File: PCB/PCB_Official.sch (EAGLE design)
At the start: 66 parts, among them IC1 MCP73871, U1 TPS63070, U2 STM32F767ZIT6, U3 STM32L053C8T6, U4 TPS63070, U5 BATTERY-MANAGEMENT-TEMP_BQ274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

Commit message: Schematic almost finalized
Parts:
- added C23, C24: 2.2uF, rcl:C-USC0805
- added C25: 10nF, rcl:C-USC0805
- added C26, C27, C28, C29, C30, C31, C32, C33, C34, C35, C36, C37, C43, C44, C45, C46, C47: 100nF, rcl:C-USC0805
- added C38: 4.7uF, rcl:C-USC0805
- added C39, C40, C41, C42: 4.3pF, rcl:C-USC0805
- added C48: 1uF, rcl:C-USC0805
- added J3: 455-1750-1-ND, SparkFun-Connectors:CONN_03
- added Q1: 220mA/50V/3.5Ω, SparkFun-DiscreteSemi:MOSFET-NCH-BSS138
- added R21, R22, R23, R24: 10k, rcl:R-US_R0805
- added SOLAR: (no value), adafruit:JST_2PIN-SMT-RA
- J1: device SparkFun-Connectors:CONN_11 -> SparkFun-Connectors:CONN_13
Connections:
- removed net N$32: J1.4
- new net DCMI_D2: J1.5, U2PC.PC8(TRACED1,TIM3_CH3,TIM8_CH3,UART5_RTS,USART6_CK,FMC_NE2/FMC_NCE,SDMMC1_D0,DCMI_D2)
- new net DCMI_D3: J1.6, U2PC.PC9(MCO2,TIM3_CH4,TIM8_CH4,I2S3_SDA,I2S_CKIN,UART5_CTS,QUADSPI_BK1_IO0,LCD_G3,SDMMC12_D1,DCMI_D3,LCD_B2)
- new net DCMI_D4: J1.7, U2PC.PC11(DFSDM1_DATIN5,SPI3_MISO,USART3_RX,UART4_RX,QUADSPI_BK2_NCS,SDMMC1_D3,DCMI_D4)
- new net DCMI_D5: J1.8, U2PD.PD3(DFSDM1_CKOUT,SPI2_SCK/I2S2_CK,DFSDM1_DATIN0,USART2_CTS,FMC_CLK,DCMI_D5,LCD_G7)
- new net DCMI_D6: J1.9, U2PB.PB8(I2C4_SCL,TIM4_CH3,TIM10_CH1,I2C1_SCL,DFSDM1_CKIN7,UART5_RX,CAN1_RX,SDMMC2_D4,ETH_MII_TXD3,SDMMC1_D4,DCMI_D6,LCD_B6)
- new net DCMI_D7: J1.10, U2PB.PB9(I2C4_SDA,TIM4_CH4,TIM11_CH1,I2C1_SDA,SPI2_NSS/I2S2_WS,DFSDM1_DATIN7,UART5_TX,CAN1_TX,SDMMC2_D5,I2C4_SMBA,SDMMC1_D5,DCMI_D7,LCD_B7)
- new net DCMI_VSYNC: J1.11, U2PG.PG9(SPI1_MISO,SPDIF_RX3,USART6_RX,QUADSPI_BK2_IO2,SAI2_FS_B,SDMMC2_D0,FMC_NE2/FMC_NCE,DCMI_VSYNC)
- new net F7_RX: MCU_UART.4, U2PA.PA1(TIM2_CH2,TIM5_CH2,USART2_RTS,UART4_RX,QUADSPI_BK1_IO3,SAI2_MCLK_B,ETH_MII_RX_CLK/ETH_RMII_REF_CLK,LCD_R2)
- new net F7_TX: MCU_UART.2, U2PA.PA0-WKUP(TIM2_CH1/TIM2_ETR,TIM5_CH1,TIM8_ETR,USART2_CTS,UART4_TX,SAI2_SD_B,ETH_MII_CRS,ADC1_IN0,ADC2_IN0,ADC3_IN0,WKUP1)
- new net GSM_RST: U$1.RST, U3.PB5
- new net I2C_SCL: J1.13, U2PB.PB6(UART5_TX,TIM4_CH1,HDMI_CEC,I2C1_SCL,DFSDM1_DATIN5,USART1_TX,CAN2_TX,QUADSPI_BK1_NCS,I2C4_SCL,FMC_SDNE1,DCMI_D5)
- new net I2C_SDA: J1.12, U2PB.PB7(TIM4_CH2,I2C1_SDA,DFSDM1_CKIN5,USART1_RX,I2C4_SDA,FMC_NL,DCMI_VSYNC)
- new net L0_RX: MCU_UART.1, U3.PB11
- new net L0_SWCLK: L0_PROGRAM.3, U3.PA14
- new net L0_SWDIO: L0_PROGRAM.2, U3.PA13
- new net L0_TX: MCU_UART.3, U3.PB10
- new net LORA_INT: U$9.G0, U3.PB6
- new net LORA_RST: U$9.RST, U3.PB7
- new net MCU_RST: J2.4, L0_PROGRAM.4, U2PWR_CONTR.NRST, U3.NRST
- new net SYS_JTCK_SWCLK: J2.3, U2PA.PA14(JTCK-SWCLK)
- new net SYS_JTMS_SWDIO: J2.2, U2PA.PA13(JTMS-SWDIO)
- new net TIM3_CH2: Q1.S, R22.1
- new net VCAP1: C23.1, U2PWR_CONTR.VCAP_1
- new net VCAP2: C24.1, U2PWR_CONTR.VCAP_2
- net +3V3: now also C25.1, C26.1, C27.1, C28.1, C29.1, C30.1, C31.1, C32.1, C33.1, C34.1, C35.1, C36.1, C37.1, C38.1, C43.1, C44.1, C45.1, C46.1, C47.1, C48.1, J2.5, L0_PROGRAM.5, Q1.G, R22.2, U2PWR_CONTR.PDR_ON, U2PWR_CONTR.VBAT, U2PWR_CONTR.VDD, U2PWR_CONTR.VDDA, U2PWR_CONTR.VDDSDMMC, U2PWR_CONTR.VDDUSB, U2PWR_CONTR.VREFP, U3.VDDA, U3.VDD_USB
- net +5V: now also J3.1, R23.2
- net BAT_SCL: now also U3.PB8
- net BAT_SDA: now also U3.PB9
- net DCMI_D1: now also J1.4
- net GND: now also C23.2, C24.2, C25.2, C26.2, C27.2, C28.2, C29.2, C30.2, C31.2, C32.2, C33.2, C34.2, C35.2, C36.2, C37.2, C38.2, C39.2, C40.2, C41.2, C42.2, C43.2, C44.2, C45.2, C46.2, C47.2, C48.2, J2.1, J3.3, L0_PROGRAM.1, R21.2, R24.1, SOLAR.1; no longer U$9.RST
- net N$23: now also R21.1, U2PWR_CONTR.BOOT0(VPP); no longer J1.11
- net N$24: now also R24.2, U3.BOOT0; no longer J1.10
- net N$27: now also C40.1, U2PH.PH1-OSC_OUT; no longer J1.9
- net N$28: now also C39.1, U2PH.PH0-OSC_IN; no longer J1.8
- net N$29: now also J3.2, Q1.D, R23.1; no longer J1.7
- net N$30: now also C42.1, U3.PH1-OSC_OUT; no longer J1.6
- net N$31: now also C41.1, U3.PH0-OSC_IN; no longer J1.5
- net VCC: now also SOLAR.2
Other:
- moved on the sheet: U2PB

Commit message: Pre-midpoint design review.
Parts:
- removed C4: 0.1uF, SparkFun-Capacitors:0.1UF-0603-25V-(+80/-20%)
- removed D2: RED, SparkFun-LED:LED-RED0603
- removed J1: (no value), SparkFun-Connectors:CONN_13
- removed R13: 2K, adafruit:R-US_FLIPFLOP
- removed R3: 10k, SparkFun-Resistors:10KOHM-0603-1/10W-1%
- removed R4: 365k, SparkFun-Resistors:365KOHM-0603-1/10W-1%
- removed R6: 1k, SparkFun-Resistors:1KOHM-0603-1/10W-1%
- removed THERM: 10K, adafruit:R-US_FLIPFLOP
- added C50: 10uF, adafruit:C-USC0805
- added C51: 0.1uF, rcl:C-USC0603
- added J4: (no value), SparkFun-Connectors:CONN_16
- added R25: 10k, adafruit:R-US_R0805
- added R26, R27: 10k, rcl:R-US_R0603
- added R28: 68.1k, rcl:R-US_R0603
- added R29: 213k, rcl:R-US_R0603
- added R30: 1k, rcl:R-US_R0603
- added RED, RED1: RED, microbuilder:LED0805_NOOUTLINE
- added U$2, U$3: 8MHZ_OSC, ForestVisionParts:8MHZ_OSC
- C1, C18: value 0.1uF -> 10uF; device SparkFun-Capacitors:0.1UF-0603-25V-(+80/-20%) -> adafruit:C-USC0805
- C12, C13, C2, C3: device SparkFun-Capacitors:10UF-0805-25V-10% -> adafruit:C-USC0805
- C14: device SparkFun-Capacitors:0.1UF-0603-25V-(+80/-20%) -> rcl:C-USC0603
- C15, C16, C17, C6: device SparkFun-Capacitors:22UF-0805-16V-20% -> adafruit:C-USC0805
- C19: value 10uF -> 4700uF/10V; device SparkFun-Capacitors:10UF-0805-25V-10% -> ForestVisionParts:ADAFRUIT_CPOL-USE5-13
- C20: value 10uF -> 0.1uF; device SparkFun-Capacitors:10UF-0805-25V-10% -> rcl:C-USC0603
- C5, C9: value 10uF -> 22uF; device SparkFun-Capacitors:10UF-0805-25V-10% -> adafruit:C-USC0805
- C7: value 22uF -> 0.1uF; device SparkFun-Capacitors:22UF-0805-16V-20% -> rcl:C-USC0603
- C8: value 22uF -> 10uF; device SparkFun-Capacitors:22UF-0805-16V-20% -> adafruit:C-USC0805
- D1: value RED -> MBR120VLSFT1GOSCT; device SparkFun-LED:LED-RED0603 -> ForestVisionParts:MICROBUILDER_DIODESOD-123
- MCU_UART: device SparkFun-Connectors:CONN_04JST-PTH -> pinhead:PINHD-1X4
- R1: value 10k -> 2k; device SparkFun-Resistors:10KOHM-0603-1/10W-1% -> adafruit:R-US_R0805
- R17: value 1k -> 10k; device SparkFun-Resistors:1KOHM-0603-1/10W-1% -> rcl:R-US_R0603
- R18: value 10k -> 68.1k; device SparkFun-Resistors:10KOHM-0603-1/10W-1% -> rcl:R-US_R0603
- R19: value 213k -> 365k; device rcl:R-US_R0805 -> rcl:R-US_R0603
- R2: value 68.1k -> 10k; device SparkFun-Resistors:68.1KOHM-0603-1/10W-1% -> adafruit:R-US_R0805
- R20: value 10k -> 1k; device rcl:R-US_R0805 -> rcl:R-US_R0603
- R5: value 68.1k -> 10k; device SparkFun-Resistors:68.1KOHM-0603-1/10W-1% -> rcl:R-US_R0603
- R7: device SparkFun-Resistors:10KOHM-0603-1/10W-1% -> adafruit:R-US_R0805
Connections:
- removed net GND_CHARGER: C10.2
- new net CLK_TBD: J4.15
- new net N$32: D1.A, SOLAR.2
- net !EN: now also R17.1; no longer R1.1
- net !EN1: now also R27.1; no longer R3.1
- net +3V3: now also C18.1, J4.16, R29.2, R30.2, R7.2; no longer C19.1, R17.2, R19.2
- net +5V: now also C3.1, C9.1, R19.2, R20.2; no longer C7.1, C8.1, R4.2, R6.2
- net DCMI_D0: now also J4.4; no longer J1.3
- net DCMI_D1: now also J4.5; no longer J1.4
- net DCMI_D2: now also J4.6; no longer J1.5
- net DCMI_D3: now also J4.7; no longer J1.6
- net DCMI_D4: now also J4.8; no longer J1.7
- net DCMI_D5: now also J4.9; no longer J1.8
- net DCMI_D6: now also J4.10; no longer J1.9
- net DCMI_D7: now also J4.11; no longer J1.10
- net DCMI_HSYNC: now also J4.2; no longer J1.1
- net DCMI_PIXCLK: now also J4.3; no longer J1.2
- net DCMI_VSYNC: now also J4.12; no longer J1.11
- net F7_RX: now also MCU_UART.1; no longer MCU_UART.4
- net F7_TX: now also MCU_UART.3; no longer MCU_UART.2
- net GND: now also C10.2, C19.-, C50.2, C51.2, J4.1, R1.1, R18.1, R25.1, R28.1, RED.C, RED1.C; no longer C19.2, C4.2, D1.C, D2.C, R13.1, R20.1, R5.1, THERM.1
- net GPOUT: now also R7.1
- net I2C_SCL: now also J4.13; no longer J1.13
- net I2C_SDA: now also J4.14; no longer J1.12
- net L0_RX: now also MCU_UART.4; no longer MCU_UART.1
- net L0_TX: now also MCU_UART.2; no longer MCU_UART.3
- net N$17: now also R1.2; no longer R13.2
- net N$19: now also R2.2; no longer THERM.2
- net N$20: now also R30.1, RED.A; no longer D2.A, R17.1
- net N$21: now also R28.2, R29.1; no longer R19.1, R5.2
- net N$26: now also R25.2; no longer R20.2
- net N$27: now also U$2.2
- net N$28: now also U$2.1
- net N$30: now also U$3.2
- net N$31: now also U$3.1
- net N$4: now also R18.2, R19.1; no longer R2.2, R4.1
- net N$5: now also R20.1, RED1.A; no longer D1.A, R6.1
- net N$6: now also C14.1; no longer C4.1
- net N$9: now also C20.1; no longer C14.1
- net PS: now also R5.1; no longer R7.1
- net PS1: now also R26.1; no longer R18.1
- net TIM3_CH2: now also U2PB.PB5(UART5_RX,TIM3_CH2,I2C1_SMBA,SPI1_MOSI/I2S1_SD,SPI3_MOSI/I2S3_SD,SPI6_MOSI,CAN2_RX,OTG_HS_ULPI_D7,ETH_PPS_OUT,FMC_SDCKE1,DCMI_D10,LCD_G7)
- net VCC: now also C19.+, D1.C; no longer SOLAR.2
- net VOUT_CHARGER: now also C50.1, C51.1, C7.1, C8.1, R17.2, R26.2, R27.2, R5.2; no longer C18.1, C20.1, C3.1, C9.1, R1.2, R18.2, R3.2, R7.2
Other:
- note added: "Camera Data Lines"
- note added: "Connectors and Servo Motors"
- note added: "Decoupling capacitors"
- note added: "Fuel Gauge"
- note added: "GSM"
- note added: "GSM Module"
- note added: "LoRa Module"
- note added: "Oscillator 8MHz"
- note added: "Programmable Headers and UART"
- note added: "STM32L053C8"
- note added: "Solar charger IC"
- note added: "Voltage Regulator (3.3 V)"
- note added: "Voltage Regulator (5 V)"
- moved on the sheet: BATT, C1, C14, C18, C20, C21, C22, C23, C24, C25, C26, C27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

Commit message: Major revision after design review
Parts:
- removed SOLAR: (no value), adafruit:JST_2PIN-SMT-RA
- added CN1: (no value), adafruit:DCBARRELPTH
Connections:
- new net LORA_EN: U$9.EN, U3.PA9
- net BAT_SCL: now also U3.PB10; no longer U3.PB8
- net BAT_SDA: now also U3.PB11; no longer U3.PB9
- net GND: now also CN1.GND, CN1.GNDBREAK; no longer SOLAR.1
- net GSM_RST: now also U3.PA4; no longer U3.PB5
- net L0_RX: now also U3.PB7; no longer U3.PB11
- net L0_TX: now also U3.PB6; no longer U3.PB10
- net LORA_INT: now also U3.PA8; no longer U3.PB6
- net LORA_RST: no longer U3.PB7
- net N$32: now also CN1.PWR; no longer SOLAR.2
- net RX_GSM: now also U3.PA3; no longer U3.PA9
- net TX_GSM: now also U3.PA2; no longer U3.PA10
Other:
- moved on the sheet: R24

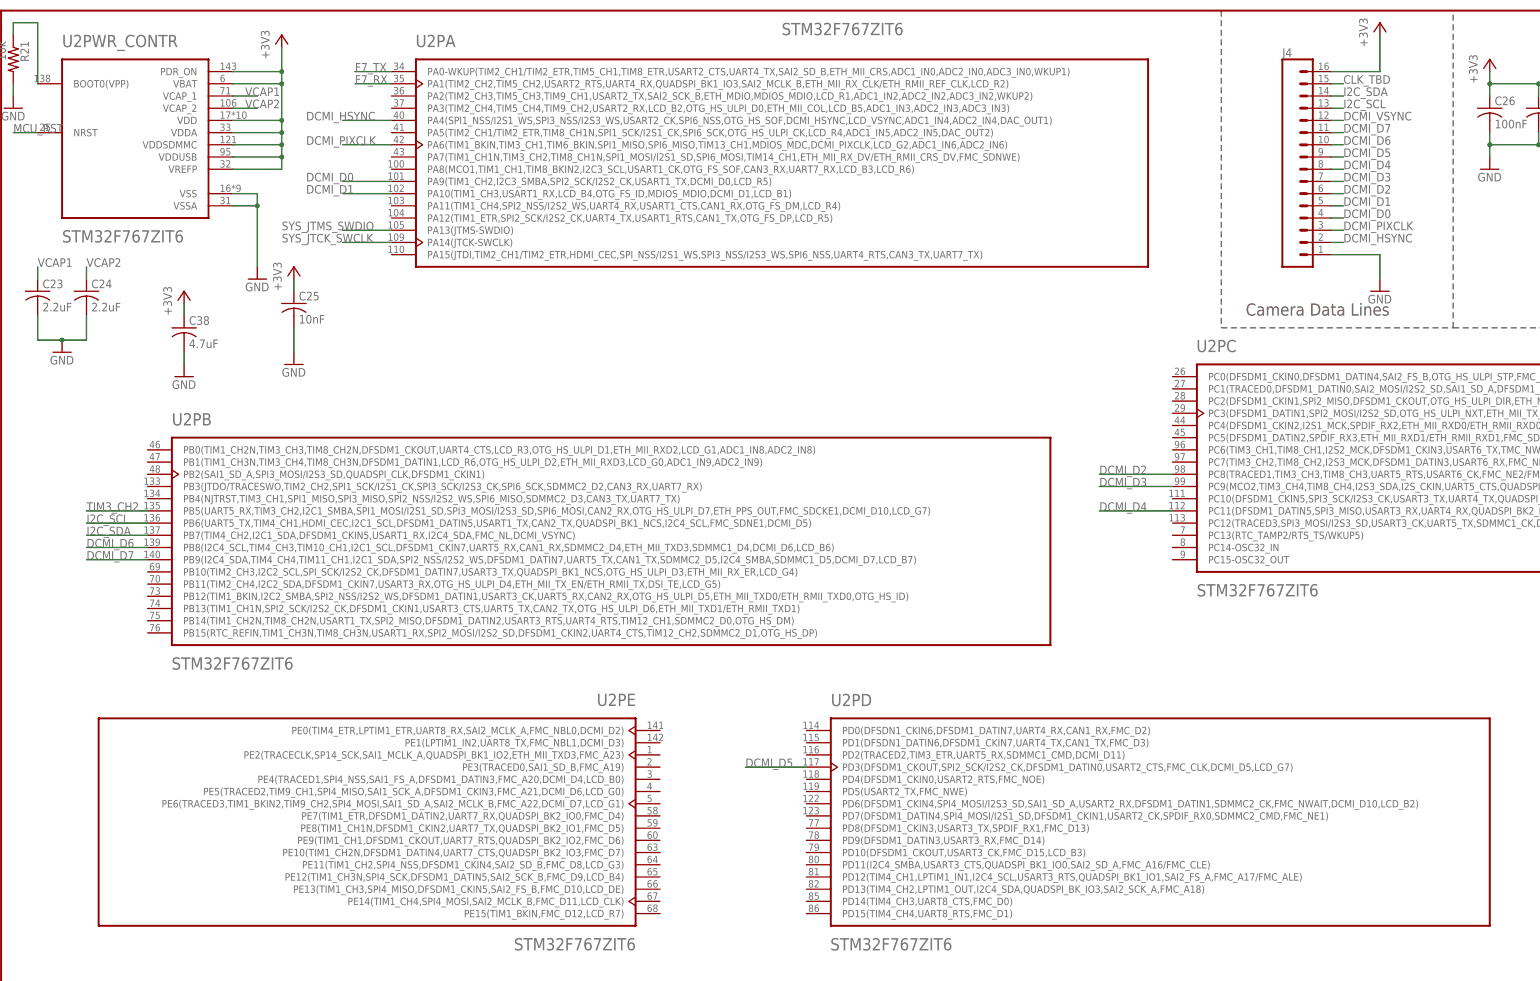
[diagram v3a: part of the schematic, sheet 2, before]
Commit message: Shuffled pin assignments for AI MCU
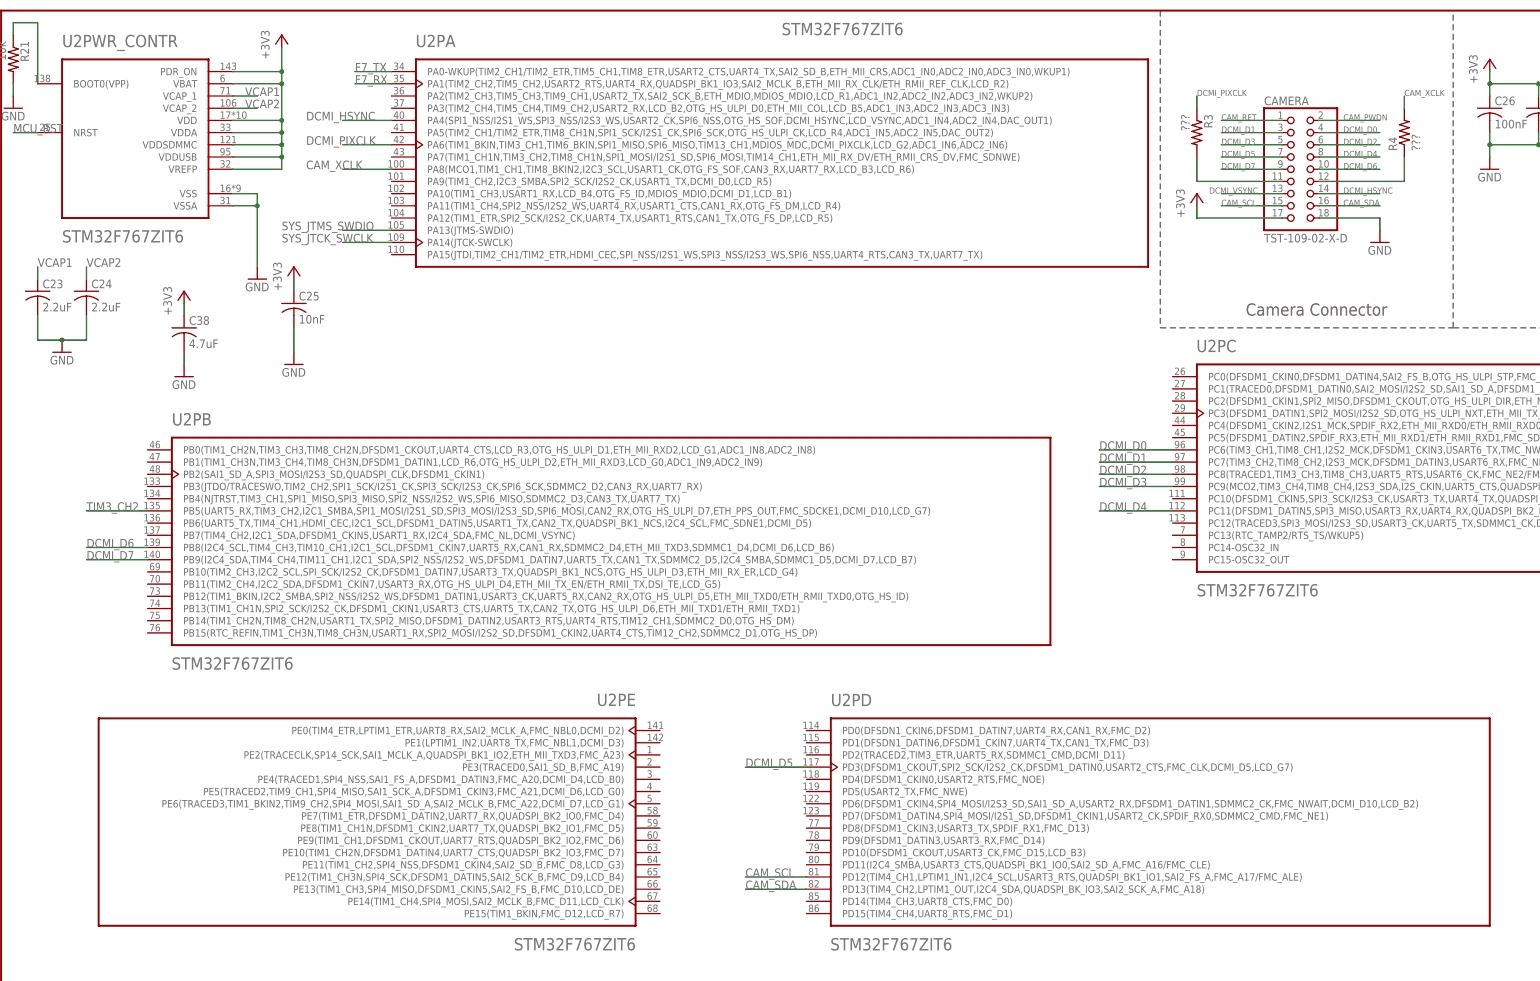
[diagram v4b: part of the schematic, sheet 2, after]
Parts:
- removed J4: (no value), SparkFun-Connectors:CONN_16
- added CAMERA: TST-109-02-X-D, ForestVisionParts:TST-109-02-X-D
- added R3, R4: ???, rcl:R-US_R0805
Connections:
- removed net CLK_TBD: J4.15
- removed net I2C_SCL: J4.13, U2PB.PB6(UART5_TX,TIM4_CH1,HDMI_CEC,I2C1_SCL,DFSDM1_DATIN5,USART1_TX,CAN2_TX,QUADSPI_BK1_NCS,I2C4_SCL,FMC_SDNE1,DCMI_D5)
- removed net I2C_SDA: J4.14, U2PB.PB7(TIM4_CH2,I2C1_SDA,DFSDM1_CKIN5,USART1_RX,I2C4_SDA,FMC_NL,DCMI_VSYNC)
- new net CAM_PWDN: CAMERA.2
- new net CAM_RET: CAMERA.1
- new net CAM_SCL: CAMERA.15, U2PD.PD12(TIM4_CH1,LPTIM1_IN1,I2C4_SCL,USART3_RTS,QUADSPI_BK1_IO1,SAI2_FS_A,FMC_A17/FMC_ALE)
- new net CAM_SDA: CAMERA.16, U2PD.PD13(TIM4_CH2,LPTIM1_OUT,I2C4_SDA,QUADSPI_BK_IO3,SAI2_SCK_A,FMC_A18)
- new net CAM_XCLK: R4.2, U2PA.PA8(MCO1,TIM1_CH1,TIM8_BKIN2,I2C3_SCL,USART1_CK,OTG_FS_SOF,CAN3_RX,UART7_RX,LCD_B3,LCD_R6)
- new net N$33: CAMERA.11, R3.2
- new net N$34: CAMERA.12, R4.1
- net +3V3: now also CAMERA.17; no longer J4.16
- net DCMI_D0: now also CAMERA.4, U2PC.PC6(TIM3_CH1,TIM8_CH1,I2S2_MCK,DFSDM1_CKIN3,USART6_TX,TMC_NWAIT,SDMMC2_D6,SDMMC1_D6,DCMI_D0,LCD_HSYNC); no longer J4.4, U2PA.PA9(TIM1_CH2,I2C3_SMBA,SPI2_SCK/I2S2_CK,USART1_TX,DCMI_D0,LCD_R5)
- net DCMI_D1: now also CAMERA.3, U2PC.PC7(TIM3_CH2,TIM8_CH2,I2S3_MCK,DFSDM1_DATIN3,USART6_RX,FMC_NE1,SDMMC2_D7,SDMMC1_D7,DCMI_D1,LCD_G6); no longer J4.5, U2PA.PA10(TIM1_CH3,USART1_RX,LCD_B4,OTG_FS_ID,MDIOS_MDIO,DCMI_D1,LCD_B1)
- net DCMI_D2: now also CAMERA.6; no longer J4.6
- net DCMI_D3: now also CAMERA.5; no longer J4.7
- net DCMI_D4: now also CAMERA.8; no longer J4.8
- net DCMI_D5: now also CAMERA.7; no longer J4.9
- net DCMI_D6: now also CAMERA.10; no longer J4.10
- net DCMI_D7: now also CAMERA.9; no longer J4.11
- net DCMI_HSYNC: now also CAMERA.14; no longer J4.2
- net DCMI_PIXCLK: now also R3.1; no longer J4.3
- net DCMI_VSYNC: now also CAMERA.13; no longer J4.12
- net GND: now also CAMERA.18; no longer J4.1
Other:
- note added: "Camera Connector"
- note removed: "Camera Data Lines"
